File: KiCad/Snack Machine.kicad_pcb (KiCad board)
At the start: 2 copper layers, 76 x 106 mm, 105 parts, among them J1 RFID_CONNECTOR, J10 Row Screw Terminal, J11 Column Screw Terminal, J12 Display Serial Header, J13 AVR-ISP-6, J2 Power Screw Terminal, J3 USB_C_Receptacle_USB2.0, J4 V2 Display Ribbon Cable, J5 MDB, J6 Conn_01x02, J9 AVR-ISP-6, Q1 P-CH 30V 3.8A, Q2 MMBT3904, Q3 MMBT3904, Q4 MMBT3904, Q5 P-CH 30V 3.8A, SW1 SW_SPST, U2 MEZD71202A-G, U3 ATmega2560-16AU, U4 TBD62783A, U5 Huzzah32, U6 ATmega16U2-MU, U7 SN74LVC1T45DBV, U8 SN74LVC1T45DBV, Y1 16MHz, Y2 16MHz

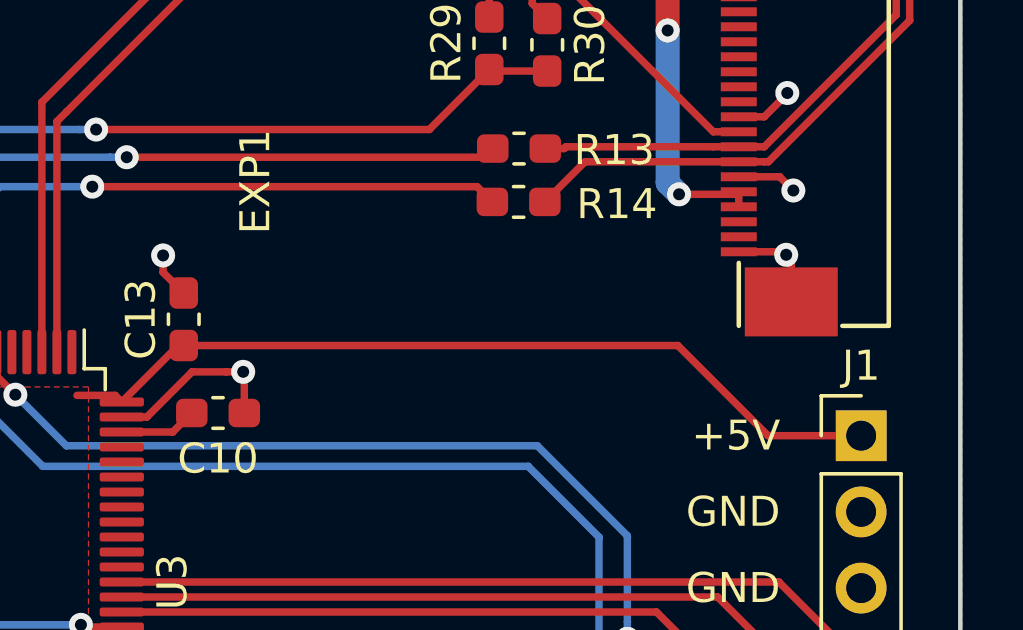
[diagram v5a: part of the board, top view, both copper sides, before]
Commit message: Fixing the +5V trace
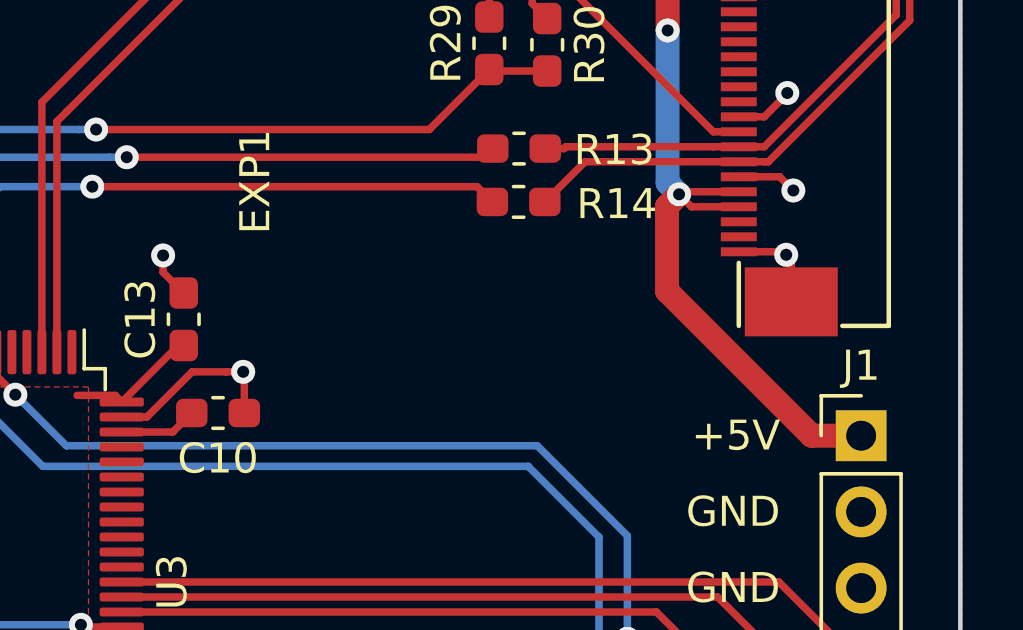
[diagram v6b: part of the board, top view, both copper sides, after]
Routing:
- net +5V: track 297.9 -> 287.6 mm
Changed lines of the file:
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@@
     (thickness 1.6)
     (drawings 24)
-    (tracks 1062)
+    (tracks 1064)
     (zones 0)
     (modules 105)
@@
     (add_net /RESET_HUZZAH)
     (add_net /RFID_BEEP_CTRL)
-    (add_net /RFID_CARD_PRESENT)
     (add_net /RFID_DATA_0)
     (add_net /RFID_DATA_1)
     (add_net /RFID_GREEN_LED)
-    (add_net /RFID_HOLD)
     (add_net /RFID_RED_LED)
     (add_net /SCK)
@@
     (add_net "Net-(D6-Pad2)")
     (add_net "Net-(D9-Pad3)")
-    (add_net "Net-(J12-Pad10)")
-    (add_net "Net-(J12-Pad2)")
-    (add_net "Net-(J12-Pad4)")
-    (add_net "Net-(J12-Pad6)")
-    (add_net "Net-(J12-Pad8)")
     (add_net "Net-(J3-PadA5)")
-    (add_net "Net-(J3-PadA8)")
     (add_net "Net-(J3-PadB5)")
-    (add_net "Net-(J3-PadB8)")
-    (add_net "Net-(J4-Pad10)")
-    (add_net "Net-(J4-Pad11)")
-    (add_net "Net-(J4-Pad12)")
-    (add_net "Net-(J4-Pad13)")
-    (add_net "Net-(J4-Pad14)")
-    (add_net "Net-(J4-Pad15)")
-    (add_net "Net-(J4-Pad16)")
-    (add_net "Net-(J4-Pad17)")
-    (add_net "Net-(J4-Pad18)")
-    (add_net "Net-(J4-Pad19)")
-    (add_net "Net-(J4-Pad2)")
-    (add_net "Net-(J4-Pad20)")
-    (add_net "Net-(J4-Pad28)")
-    (add_net "Net-(J4-Pad29)")
-    (add_net "Net-(J4-Pad3)")
-    (add_net "Net-(J4-Pad4)")
-    (add_net "Net-(J4-Pad5)")
-    (add_net "Net-(J4-Pad6)")
-    (add_net "Net-(J4-Pad7)")
-    (add_net "Net-(J4-Pad8)")
-    (add_net "Net-(J4-Pad9)")
-    (add_net "Net-(J5-Pad3)")
     (add_net "Net-(J5-Pad5)")
     (add_net "Net-(Q2-Pad1)")
@@
     (add_net "Net-(R36-Pad2)")
     (add_net "Net-(R7-Pad2)")
-    (add_net "Net-(U3-Pad1)")
-    (add_net "Net-(U3-Pad15)")
-    (add_net "Net-(U3-Pad16)")
-    (add_net "Net-(U3-Pad17)")
-    (add_net "Net-(U3-Pad19)")
-    (add_net "Net-(U3-Pad23)")
-    (add_net "Net-(U3-Pad24)")
-    (add_net "Net-(U3-Pad25)")
-    (add_net "Net-(U3-Pad26)")
-    (add_net "Net-(U3-Pad27)")
-    (add_net "Net-(U3-Pad28)")
-    (add_net "Net-(U3-Pad29)")
-    (add_net "Net-(U3-Pad4)")
-    (add_net "Net-(U3-Pad43)")
-    (add_net "Net-(U3-Pad47)")
-    (add_net "Net-(U3-Pad48)")
-    (add_net "Net-(U3-Pad49)")
-    (add_net "Net-(U3-Pad5)")
-    (add_net "Net-(U3-Pad50)")
-    (add_net "Net-(U3-Pad51)")
-    (add_net "Net-(U3-Pad52)")
-    (add_net "Net-(U3-Pad65)")
-    (add_net "Net-(U3-Pad66)")
-    (add_net "Net-(U3-Pad68)")
-    (add_net "Net-(U3-Pad69)")
-    (add_net "Net-(U3-Pad70)")
-    (add_net "Net-(U3-Pad71)")
-    (add_net "Net-(U3-Pad72)")
-    (add_net "Net-(U3-Pad73)")
-    (add_net "Net-(U3-Pad74)")
-    (add_net "Net-(U3-Pad75)")
-    (add_net "Net-(U3-Pad76)")
-    (add_net "Net-(U3-Pad77)")
-    (add_net "Net-(U3-Pad78)")
-    (add_net "Net-(U3-Pad79)")
-    (add_net "Net-(U3-Pad8)")
-    (add_net "Net-(U3-Pad82)")
-    (add_net "Net-(U3-Pad83)")
-    (add_net "Net-(U3-Pad84)")
-    (add_net "Net-(U3-Pad89)")
-    (add_net "Net-(U3-Pad9)")
-    (add_net "Net-(U3-Pad90)")
-    (add_net "Net-(U3-Pad91)")
-    (add_net "Net-(U3-Pad92)")
-    (add_net "Net-(U3-Pad93)")
-    (add_net "Net-(U3-Pad94)")
-    (add_net "Net-(U3-Pad95)")
-    (add_net "Net-(U3-Pad96)")
-    (add_net "Net-(U3-Pad97)")
-    (add_net "Net-(U5-Pad1)")
-    (add_net "Net-(U5-Pad10)")
-    (add_net "Net-(U5-Pad11)")
-    (add_net "Net-(U5-Pad12)")
-    (add_net "Net-(U5-Pad13)")
     (add_net "Net-(U5-Pad14)")
     (add_net "Net-(U5-Pad15)")
-    (add_net "Net-(U5-Pad16)")
-    (add_net "Net-(U5-Pad17)")
-    (add_net "Net-(U5-Pad18)")
-    (add_net "Net-(U5-Pad19)")
-    (add_net "Net-(U5-Pad2)")
-    (add_net "Net-(U5-Pad20)")
-    (add_net "Net-(U5-Pad21)")
-    (add_net "Net-(U5-Pad22)")
-    (add_net "Net-(U5-Pad23)")
-    (add_net "Net-(U5-Pad24)")
-    (add_net "Net-(U5-Pad26)")
-    (add_net "Net-(U5-Pad4)")
-    (add_net "Net-(U5-Pad5)")
-    (add_net "Net-(U5-Pad6)")
-    (add_net "Net-(U5-Pad7)")
-    (add_net "Net-(U5-Pad8)")
-    (add_net "Net-(U5-Pad9)")
-    (add_net "Net-(U6-Pad12)")
-    (add_net "Net-(U6-Pad14)")
-    (add_net "Net-(U6-Pad18)")
-    (add_net "Net-(U6-Pad19)")
-    (add_net "Net-(U6-Pad20)")
-    (add_net "Net-(U6-Pad21)")
-    (add_net "Net-(U6-Pad22)")
-    (add_net "Net-(U6-Pad23)")
-    (add_net "Net-(U6-Pad25)")
-    (add_net "Net-(U6-Pad26)")
-    (add_net "Net-(U6-Pad5)")
-    (add_net "Net-(U6-Pad6)")
-    (add_net "Net-(U6-Pad7)")
   )
   (net_class "High Amp" ""
@@
   (segment (start 162.292 113.778) (end 164.084 115.57) (width 0.25) (layer F.Cu) (net 5))
   (segment (start 162.292 113.665) (end 162.292 113.778) (width 0.25) (layer F.Cu) (net 5))
-  (segment (start 150.114 95.4646) (end 166.5846 95.4646) (width 0.25) (layer F.Cu) (net 5))
-  (segment (start 166.5846 95.4646) (end 169.5908 98.4708) (width 0.25) (layer F.Cu) (net 5))
-  (segment (start 169.5908 98.4708) (end 172.6948 98.4708) (width 0.25) (layer F.Cu) (net 5))
-  (segment (start 168.615 90.84) (end 168.615 90.34) (width 0.25) (layer F.Cu) (net 5))
   (segment (start 169.6154 71.9074) (end 169.5196 71.9074) (width 0.8) (layer F.Cu) (net 5))
   (segment (start 169.5196 71.9074) (end 166.243 75.184) (width 0.8) (layer F.Cu) (net 5))
@@
   (segment (start 166.243 90.043) (end 166.624 90.424) (width 0.8) (layer B.Cu) (net 5))
   (segment (start 166.243 84.963) (end 166.243 90.043) (width 0.8) (layer B.Cu) (net 5))
-  (segment (start 168.531 90.424) (end 168.615 90.34) (width 0.25) (layer F.Cu) (net 5))
-  (segment (start 166.624 90.424) (end 168.531 90.424) (width 0.25) (layer F.Cu) (net 5))
+  (segment (start 171.0448 98.4708) (end 172.6948 98.4708) (width 0.8) (layer F.Cu) (net 5))
+  (segment (start 166.224001 93.650001) (end 171.0448 98.4708) (width 0.8) (layer F.Cu) (net 5))
+  (segment (start 166.224001 90.823999) (end 166.224001 93.650001) (width 0.8) (layer F.Cu) (net 5))
+  (segment (start 166.624 90.424) (end 166.224001 90.823999) (width 0.8) (layer F.Cu) (net 5))
+  (segment (start 167.04 90.84) (end 166.624 90.424) (width 0.25) (layer F.Cu) (net 5))
+  (segment (start 168.615 90.84) (end 167.04 90.84) (width 0.25) (layer F.Cu) (net 5))
+  (segment (start 166.708 90.34) (end 166.624 90.424) (width 0.25) (layer F.Cu) (net 5))
+  (segment (start 168.615 90.34) (end 166.708 90.34) (width 0.25) (layer F.Cu) (net 5))
   (segment (start 150.9338 54.5542) (end 151.0794 54.5542) (width 0.25) (layer B.Cu) (net 6))
   (via (at 151.0794 54.5542) (size 0.8) (drill 0.4) (layers F.Cu B.Cu) (net 6))

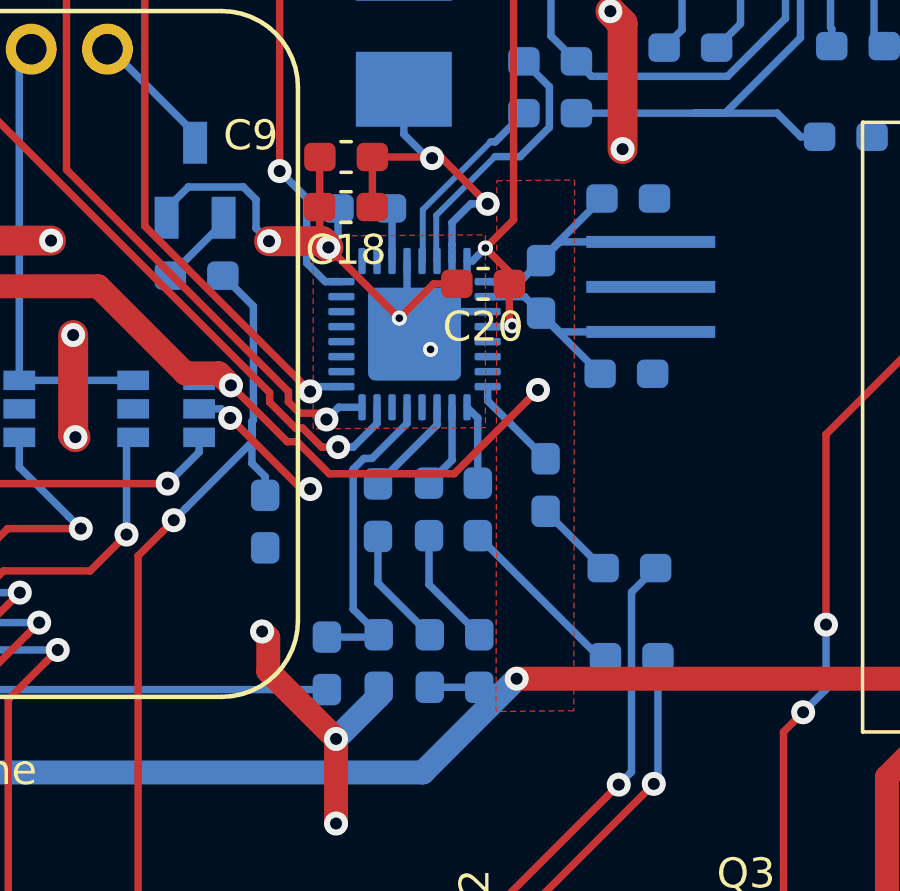
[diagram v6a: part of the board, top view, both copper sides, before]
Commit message: Improving some grounding issues
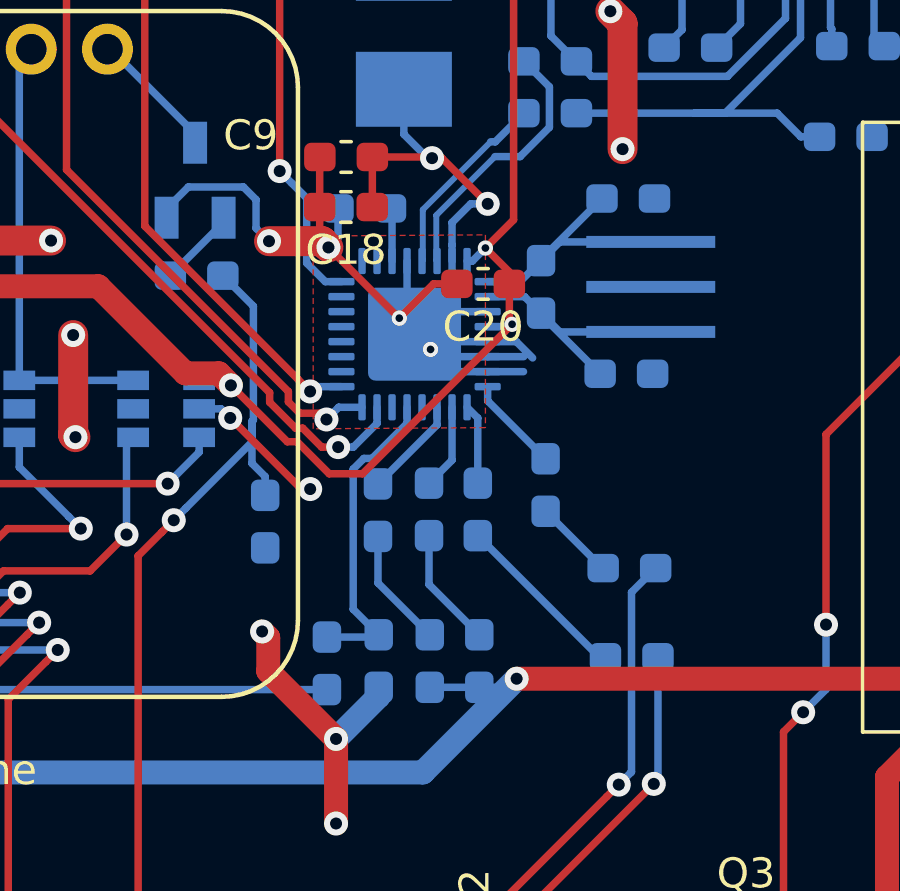
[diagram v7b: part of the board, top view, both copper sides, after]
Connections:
- U6 pad 5: (no net) -> GND
- U6 pad 6: (no net) -> GND
- U6 pad 7: (no net) -> GND
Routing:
- net GND: track 160.8 -> 173.1 mm
- net +5V: vias 12 -> 11

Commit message: Committing changes to the circuit board
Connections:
- J1 pad 10: (no net) -> /RFID_CARD_PRESENT
- J1 pad 7: (no net) -> /RFID_HOLD
- J12 pad 10: (no net) -> Net-(J12-Pad10)
- J12 pad 2: (no net) -> Net-(J12-Pad2)
- J12 pad 4: (no net) -> Net-(J12-Pad4)
- J12 pad 6: (no net) -> Net-(J12-Pad6)
- J12 pad 8: (no net) -> Net-(J12-Pad8)
- J3 pad A8: (no net) -> Net-(J3-PadA8)
- J3 pad B8: (no net) -> Net-(J3-PadB8)
- J4 pad 10: (no net) -> Net-(J4-Pad10)
- J4 pad 11: (no net) -> Net-(J4-Pad11)
- J4 pad 12: (no net) -> Net-(J4-Pad12)
- J4 pad 13: (no net) -> Net-(J4-Pad13)
- J4 pad 14: (no net) -> Net-(J4-Pad14)
- J4 pad 15: (no net) -> Net-(J4-Pad15)
- J4 pad 16: (no net) -> Net-(J4-Pad16)
- J4 pad 17: (no net) -> Net-(J4-Pad17)
- J4 pad 18: (no net) -> Net-(J4-Pad18)
- J4 pad 19: (no net) -> Net-(J4-Pad19)
- J4 pad 2: (no net) -> Net-(J4-Pad2)
- J4 pad 20: (no net) -> Net-(J4-Pad20)
- J4 pad 28: (no net) -> Net-(J4-Pad28)
- J4 pad 29: (no net) -> Net-(J4-Pad29)
- J4 pad 3: (no net) -> Net-(J4-Pad3)
- J4 pad 4: (no net) -> Net-(J4-Pad4)
- J4 pad 5: (no net) -> Net-(J4-Pad5)
- J4 pad 6: (no net) -> Net-(J4-Pad6)
- J4 pad 7: (no net) -> Net-(J4-Pad7)
- J4 pad 8: (no net) -> Net-(J4-Pad8)
- J4 pad 9: (no net) -> Net-(J4-Pad9)
- J5 pad 3: (no net) -> Net-(J5-Pad3)
- U3 pad 1: (no net) -> Net-(U3-Pad1)
- U3 pad 15: (no net) -> Net-(U3-Pad15)
- U3 pad 16: (no net) -> Net-(U3-Pad16)
- U3 pad 17: (no net) -> Net-(U3-Pad17)
- U3 pad 19: (no net) -> Net-(U3-Pad19)
- U3 pad 23: (no net) -> Net-(U3-Pad23)
- U3 pad 24: (no net) -> Net-(U3-Pad24)
- U3 pad 25: (no net) -> Net-(U3-Pad25)
- U3 pad 26: (no net) -> Net-(U3-Pad26)
- U3 pad 27: (no net) -> Net-(U3-Pad27)
- U3 pad 28: (no net) -> Net-(U3-Pad28)
- U3 pad 29: (no net) -> Net-(U3-Pad29)
- U3 pad 4: (no net) -> Net-(U3-Pad4)
- U3 pad 43: (no net) -> Net-(U3-Pad43)
- U3 pad 47: (no net) -> Net-(U3-Pad47)
- U3 pad 48: (no net) -> Net-(U3-Pad48)
- U3 pad 49: (no net) -> Net-(U3-Pad49)
- U3 pad 5: (no net) -> Net-(U3-Pad5)
- U3 pad 50: (no net) -> Net-(U3-Pad50)
- U3 pad 51: (no net) -> Net-(U3-Pad51)
- U3 pad 52: (no net) -> Net-(U3-Pad52)
- U3 pad 65: (no net) -> Net-(U3-Pad65)
- U3 pad 66: (no net) -> Net-(U3-Pad66)
- U3 pad 68: (no net) -> Net-(U3-Pad68)
- U3 pad 69: (no net) -> Net-(U3-Pad69)
- U3 pad 70: (no net) -> Net-(U3-Pad70)
- U3 pad 71: (no net) -> Net-(U3-Pad71)
- U3 pad 72: (no net) -> Net-(U3-Pad72)
- U3 pad 73: (no net) -> Net-(U3-Pad73)
- U3 pad 74: (no net) -> Net-(U3-Pad74)
- U3 pad 75: (no net) -> Net-(U3-Pad75)
- U3 pad 76: (no net) -> Net-(U3-Pad76)
- U3 pad 77: (no net) -> Net-(U3-Pad77)
- U3 pad 78: (no net) -> Net-(U3-Pad78)
- U3 pad 79: (no net) -> Net-(U3-Pad79)
- U3 pad 8: (no net) -> Net-(U3-Pad8)
- U3 pad 82: (no net) -> Net-(U3-Pad82)
- U3 pad 83: (no net) -> Net-(U3-Pad83)
- U3 pad 84: (no net) -> Net-(U3-Pad84)
- U3 pad 89: (no net) -> Net-(U3-Pad89)
- U3 pad 9: (no net) -> Net-(U3-Pad9)
- U3 pad 90: (no net) -> Net-(U3-Pad90)
- U3 pad 91: (no net) -> Net-(U3-Pad91)
- U3 pad 92: (no net) -> Net-(U3-Pad92)
- U3 pad 93: (no net) -> Net-(U3-Pad93)
- U3 pad 94: (no net) -> Net-(U3-Pad94)
- U3 pad 95: (no net) -> Net-(U3-Pad95)
- U3 pad 96: (no net) -> Net-(U3-Pad96)
- U3 pad 97: (no net) -> Net-(U3-Pad97)
- U5 pad 1: (no net) -> Net-(U5-Pad1)
- U5 pad 10: (no net) -> Net-(U5-Pad10)
- U5 pad 11: (no net) -> Net-(U5-Pad11)
- U5 pad 12: (no net) -> Net-(U5-Pad12)
- U5 pad 13: (no net) -> Net-(U5-Pad13)
- U5 pad 16: (no net) -> Net-(U5-Pad16)
- U5 pad 17: (no net) -> Net-(U5-Pad17)
- U5 pad 18: (no net) -> Net-(U5-Pad18)
- U5 pad 19: (no net) -> Net-(U5-Pad19)
- U5 pad 2: (no net) -> Net-(U5-Pad2)
- U5 pad 20: (no net) -> Net-(U5-Pad20)
- U5 pad 21: (no net) -> Net-(U5-Pad21)
- U5 pad 22: (no net) -> Net-(U5-Pad22)
- U5 pad 23: (no net) -> Net-(U5-Pad23)
- U5 pad 24: (no net) -> Net-(U5-Pad24)
- U5 pad 26: (no net) -> Net-(U5-Pad26)
- U5 pad 4: (no net) -> Net-(U5-Pad4)
- U5 pad 5: (no net) -> Net-(U5-Pad5)
- U5 pad 6: (no net) -> Net-(U5-Pad6)
- U5 pad 7: (no net) -> Net-(U5-Pad7)
- U5 pad 8: (no net) -> Net-(U5-Pad8)
- U5 pad 9: (no net) -> Net-(U5-Pad9)
- U6 pad 12: (no net) -> Net-(U6-Pad12)
- U6 pad 14: (no net) -> Net-(U6-Pad14)
- U6 pad 18: (no net) -> Net-(U6-Pad18)
- U6 pad 19: (no net) -> Net-(U6-Pad19)
- U6 pad 20: (no net) -> Net-(U6-Pad20)
- U6 pad 21: (no net) -> Net-(U6-Pad21)
- U6 pad 22: (no net) -> Net-(U6-Pad22)
- U6 pad 23: (no net) -> Net-(U6-Pad23)
- U6 pad 25: (no net) -> Net-(U6-Pad25)
- U6 pad 26: (no net) -> Net-(U6-Pad26)
